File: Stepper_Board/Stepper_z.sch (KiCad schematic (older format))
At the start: 14 parts

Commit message: Testsoftware for ImageProcessing in c programmiert
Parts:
- removed C?: 2.2u 16V, Capacitor_SMD:C_0603_1608Metric, symbol Device:C_Small
- removed C? (x4): 100n 50V, Capacitor_SMD:C_0603_1608Metric, symbol Device:C_Small
- removed C? (x2): 100u 35V, Capacitor_THT:CP_Radial_D6.3mm_P2.50mm, symbol Device:CP_Small
- removed C?: 1u 16V, Capacitor_SMD:C_0603_1608Metric, symbol Device:C_Small
- removed R? (x2): 0.1R 0.5W, Resistor_SMD:R_1210_3225Metric, symbol Device:R_Small
- removed R?: 22k, Resistor_SMD:R_0603_1608Metric, symbol Device:R_Small
- removed SW?: SW_DIP_x03, Package_DIP:DIP-6_W7.62mm, symbol Switch:SW_DIP_x03
- removed U?: TMC2226, Package_SO:TSSOP-28-1EP_4.4x9.7mm_P0.65mm, symbol Pick_n_Place:TMC2226
- added C401, C405, C406, C407: 100n 50V, Capacitor_SMD:C_0603_1608Metric, symbol Device:C_Small
- added C402: 2.2u 16V, Capacitor_SMD:C_0603_1608Metric, symbol Device:C_Small
- added C403: 1u 16V, Capacitor_SMD:C_0603_1608Metric, symbol Device:C_Small
- added C408, C409: 100u 35V, Capacitor_THT:CP_Radial_D6.3mm_P2.50mm, symbol Device:CP_Small
- added R401: 22k, Resistor_SMD:R_0603_1608Metric, symbol Device:R_Small
- added R402, R403: 0.1R 0.5W, Resistor_SMD:R_1210_3225Metric, symbol Device:R_Small
- added SW401: SW_DIP_x03, Package_DIP:DIP-6_W7.62mm, symbol Switch:SW_DIP_x03
- added U401: TMC2226-Pick_n_Place, Package_SO:TSSOP-28-1EP_4.4x9.7mm_P0.65mm, symbol StepperBoard-rescue:TMC2226-Pick_n_Place
- gave numbers to parts that had none: 1

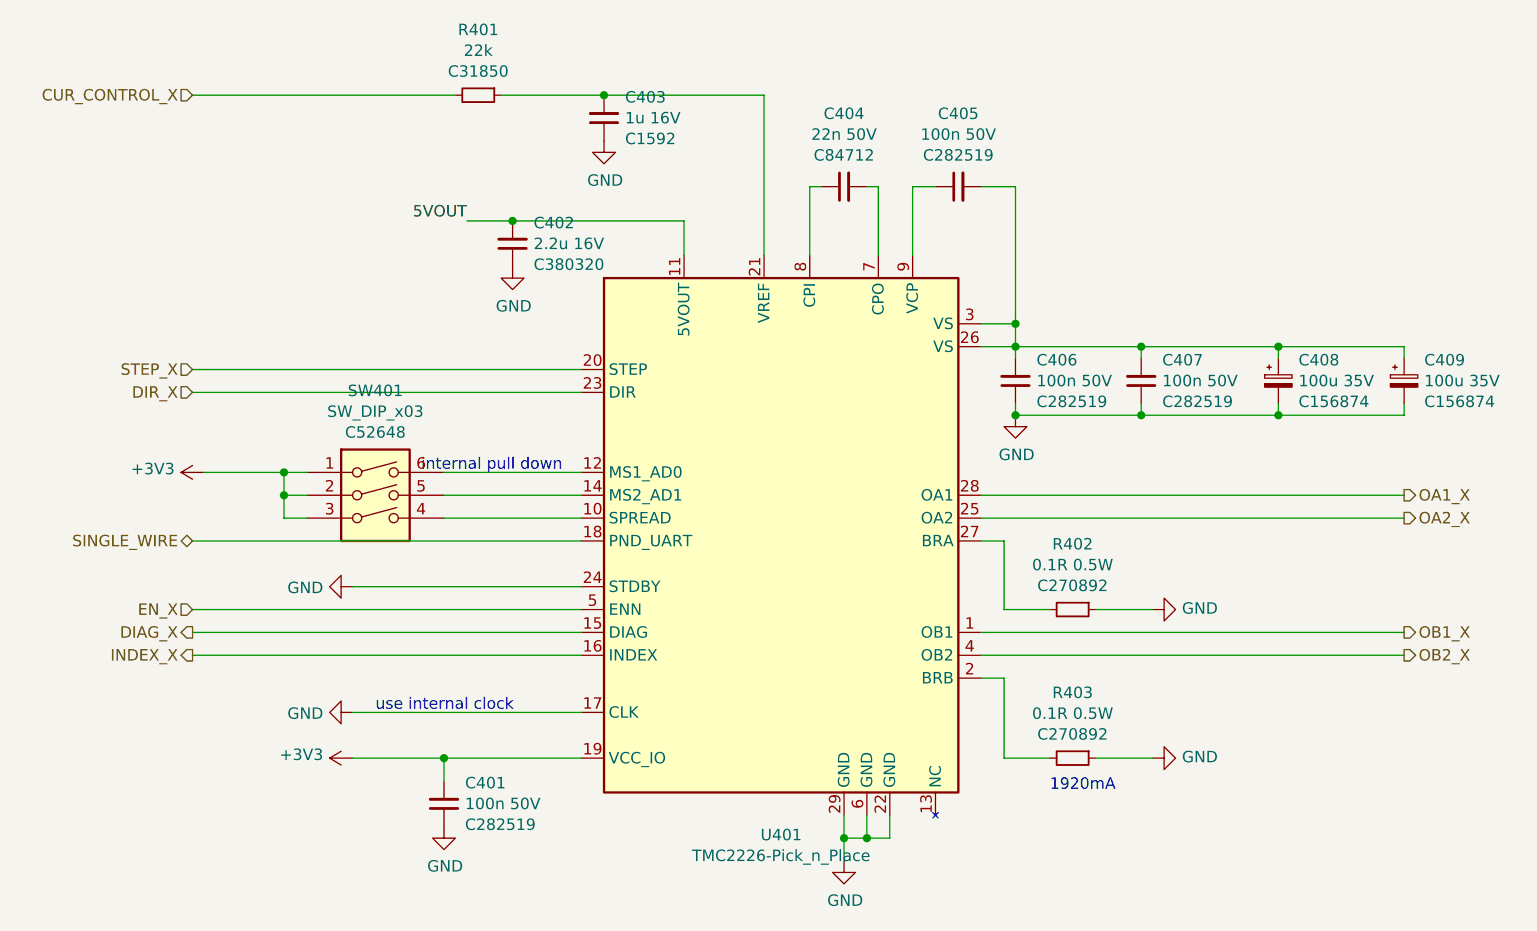
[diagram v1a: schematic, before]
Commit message: STM32F401 für motoransteuerung gewählt. TODO: motoransteuerung und leistungsteil trennen, damit für schnelle fehlerbehebung modul getauscht werden kann
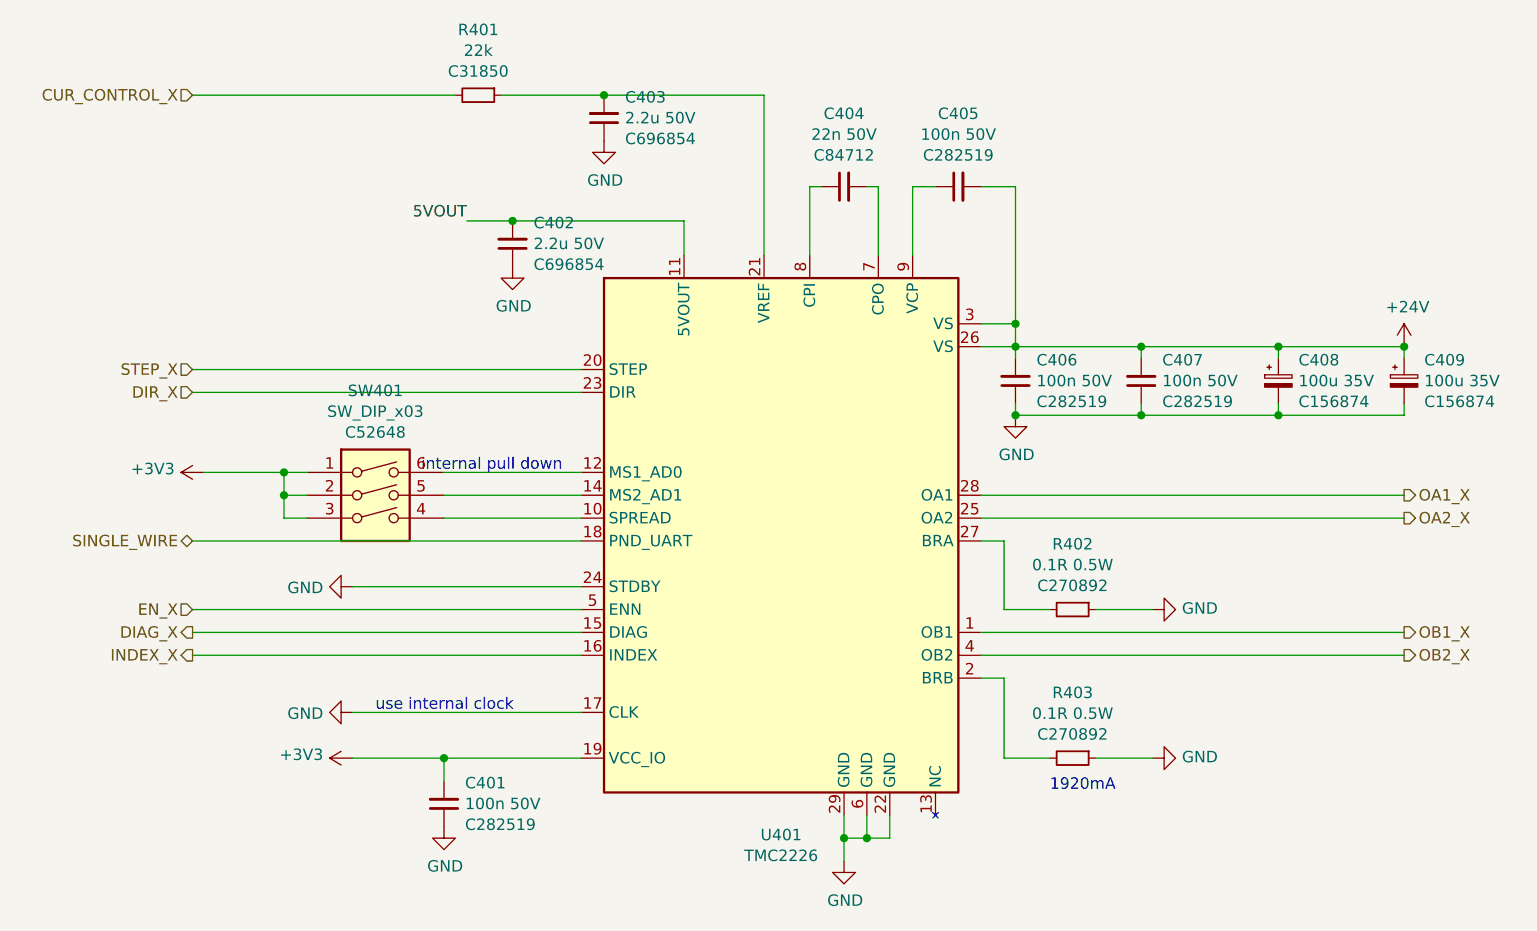
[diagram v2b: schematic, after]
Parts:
- C402: value 2.2u 16V -> 2.2u 50V; footprint Capacitor_SMD:C_0603_1608Metric -> Capacitor_SMD:C_1210_3225Metric; LCSC C380320 -> C696854
- C403: value 1u 16V -> 2.2u 50V; footprint Capacitor_SMD:C_0603_1608Metric -> Capacitor_SMD:C_1210_3225Metric; LCSC C1592 -> C696854
- U401: value TMC2226-Pick_n_Place -> TMC2226; LCSC (none) -> C705366
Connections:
- net +24V: now reaches C405.2, C406.2, C407.2, C408.1, C409.1, U401.26 (VS), U401.3 (VS)
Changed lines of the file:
@@
 AR Path="/5FCB2242/5FCB6217" Ref="C?"  Part="1"
 F 0 "C402" H 5458 1509 50  0000 R CNN
-F 1 "2.2u 16V" H 5458 1600 50  0000 R CNN
-F 2 "Capacitor_SMD:C_0603_1608Metric" H 5550 1600 50  0001 C CNN
+F 1 "2.2u 50V" H 5458 1600 50  0000 R CNN
+F 2 "Capacitor_SMD:C_1210_3225Metric" H 5550 1600 50  0001 C CNN
 F 3 "~" H 5550 1600 50  0001 C CNN
-F 4 "C380320 " H 5458 1691 50  0000 R CNN "LCSC"
+F 4 " C696854 " H 5458 1691 50  0000 R CNN "LCSC"
 	1    5550 1600
 	-1   0    0    1
@@
 AR Path="/5FCB2242/5FCB6244" Ref="C?"  Part="1"
 F 0 "C403" H 5858 959 50  0000 R CNN
-F 1 "1u 16V" H 5858 1050 50  0000 R CNN
-F 2 "Capacitor_SMD:C_0603_1608Metric" H 5950 1050 50  0001 C CNN
+F 1 "2.2u 50V" H 5858 1050 50  0000 R CNN
+F 2 "Capacitor_SMD:C_1210_3225Metric" H 5950 1050 50  0001 C CNN
 F 3 "~" H 5950 1050 50  0001 C CNN
-F 4 "C1592" H 5858 1141 50  0000 R CNN "LCSC"
+F 4 " C696854 " H 5858 1141 50  0000 R CNN "LCSC"
 	1    5950 1050
 	-1   0    0    1
@@
 AR Path="/5FCB2242/5FCB2199" Ref="U?"  Part="1"
 F 0 "U401" H 6725 1114 50  0000 C CNN
-F 1 "TMC2226-Pick_n_Place" H 6725 1023 50  0000 C CNN
+F 1 "TMC2226" H 6725 1023 50  0000 C CNN
 F 2 "Package_SO:TSSOP-28-1EP_4.4x9.7mm_P0.65mm" H 6700 850 50  0001 C CNN
 F 3 "" H 5300 3700 50  0001 C CNN
+F 4 "C705366" H 0   0   50  0001 C CNN "LCSC"
 	1    6450 2650
 	1    0    0    -1
 $EndComp
+$Comp
+L power:+24V #PWR0401
+U 1 1 60051F01
+P 9450 2050
+F 0 "#PWR0401" H 9450 1900 50  0001 C CNN
+F 1 "+24V" H 9465 2223 50  0000 C CNN
+F 2 "" H 9450 2050 50  0001 C CNN
+F 3 "" H 9450 2050 50  0001 C CNN
+	1    9450 2050
+	1    0    0    -1
+$EndComp
+Connection ~ 9450 2050
 $EndSCHEMATC
